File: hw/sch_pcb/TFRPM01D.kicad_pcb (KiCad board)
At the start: 2 copper layers, 37.5 x 19 mm, 23 parts, among them J1 HEADER_1x03, J2 SM04B-GHS-TB, J3 SM04B-GHS-TB, M2 M3, U1 PCF8583, U2 74HC1G14GW, U3 MIC5504-3.3YM5

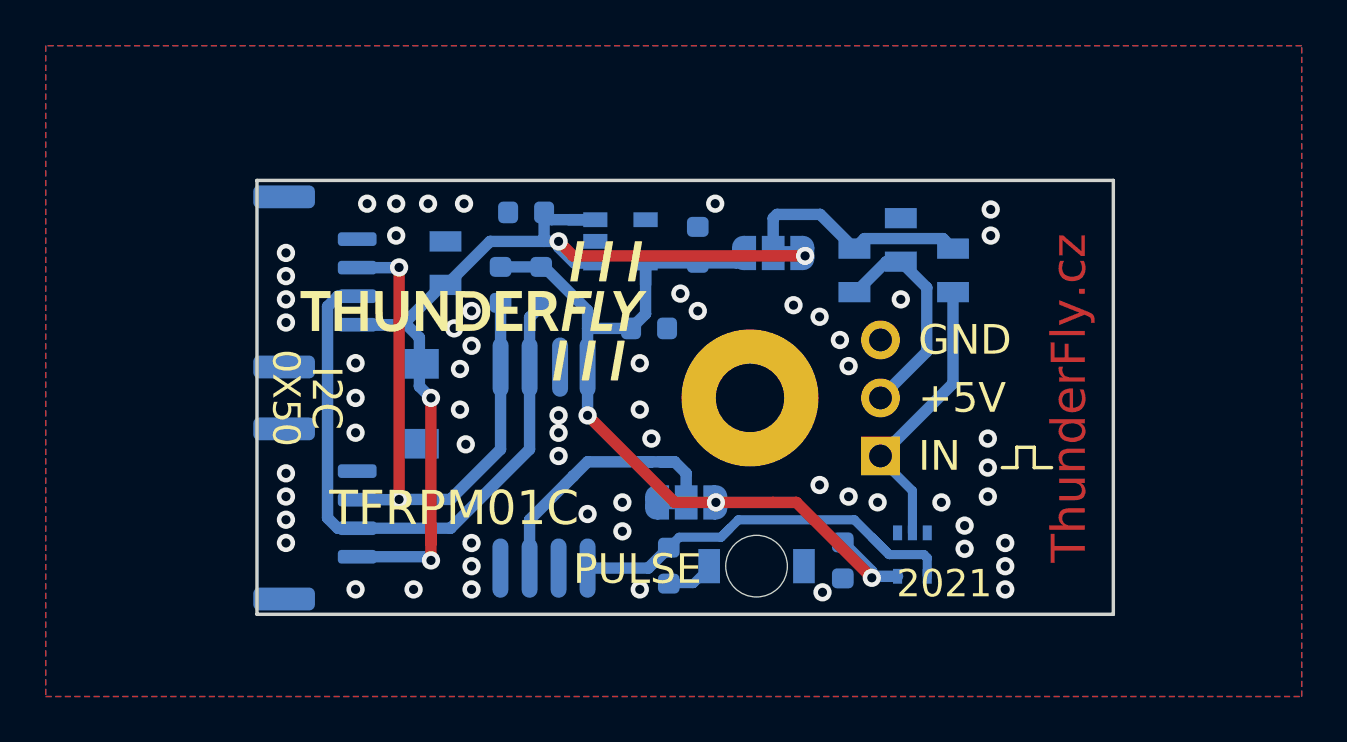
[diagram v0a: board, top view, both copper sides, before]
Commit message: Upraveni PCB, pridani popisku, vyresení #21, #26, urava silkscreenu, vypocet polohy led v openscadu
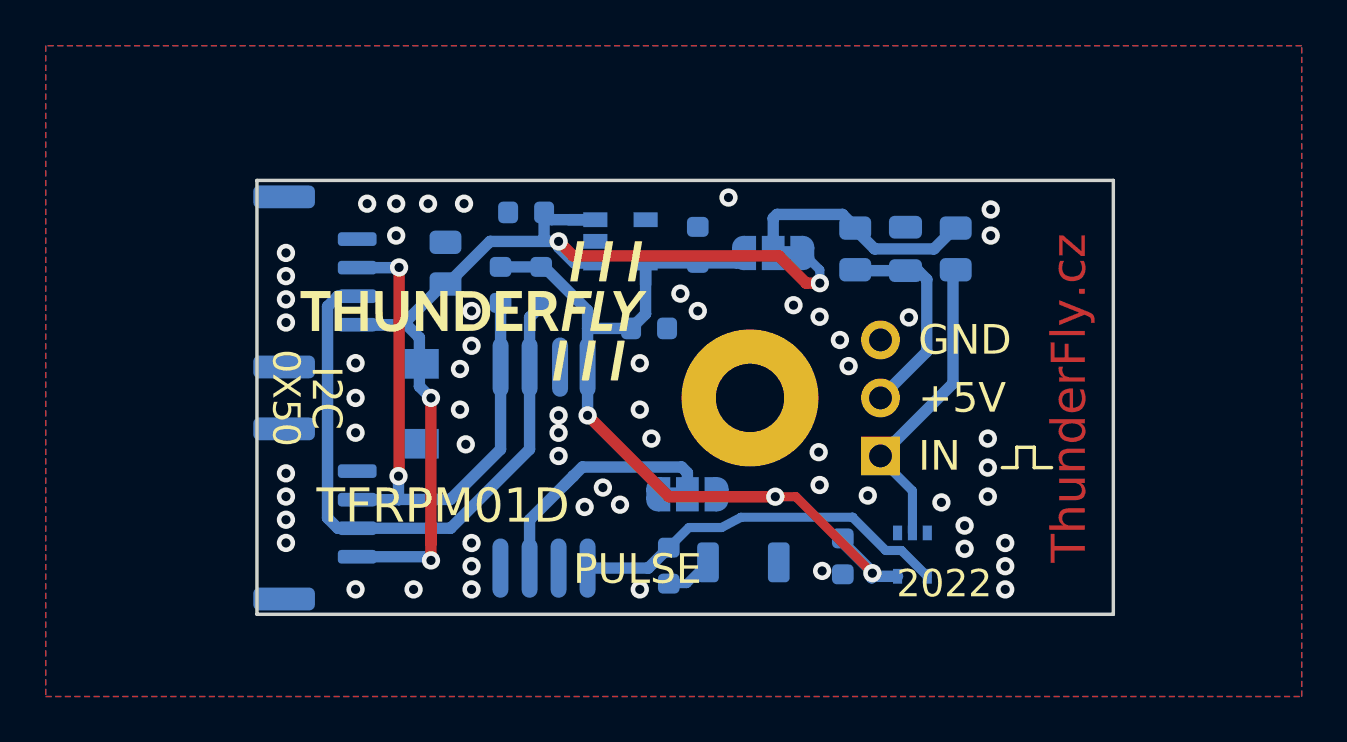
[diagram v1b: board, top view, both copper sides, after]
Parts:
- C2: footprint Mlab_R:SMD-0805 -> Capacitor_SMD:C_0805_2012Metric
- C3, R1, R2: footprint Mlab_R:SMD-0805 -> Resistor_SMD:R_0805_2012Metric
- D1: footprint Mlab_D:Diode-MiniMELF_Standard -> Diode_SMD:D_MiniMELF
- D2: footprint Mlab_D:LED_1206 -> LED_SMD:LED_1206_3216Metric_ReverseMount_Hole1.8x2.4mm
- moved R1 0.95 mm to (141.6, 125.8)
- moved R2 0.94 mm to (137.2, 125.8)
- moved D2 0.60 mm to (132.3, 139.5), turned to 180 degrees
- moved C2 0.44 mm to (139.4, 125.8)
- moved JP1 0.36 mm to (129.8, 136.5)
- moved C6 0.18 mm to (136.7, 139.3)
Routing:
- net +5V: track 45.8 -> 48.6 mm
- net +3V3: track 38.4 -> 40.9 mm
- net Net-(JP1-Pad2): track 13.9 -> 11.7 mm
- net Net-(R4-Pad1): track 18.9 -> 17.1 mm
- net /COUNT: track 12.6 -> 13.6 mm
- net Net-(C2-Pad1): track 9.86 -> 9.32 mm
- net GND: vias 60 -> 59
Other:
- board text added: "2022"
- board text added: "5V"
- board text added: "TFRPM01D"
- board text removed: "2021"
- board text removed: "TFRPM01C"

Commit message: update action, clean repo
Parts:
- removed G***: LOGO, MLAB_LOGA:TF
- added D3: LED GREEN, Diode_SMD:D_1206_3216Metric, B.Cu at (122.3, 139.5)
- added R5: R, Resistor_SMD:R_0603_1608Metric, B.Cu at (127.3, 139.7)
- C1, C4, C5, C6: footprint Mlab_R:SMD-0603 -> Capacitor_SMD:C_0603_1608Metric
- C3: footprint Resistor_SMD:R_0805_2012Metric -> Capacitor_SMD:C_0805_2012Metric
- D1: value ZENER-5.6V -> ZENER-6.2V
- D2: footprint LED_SMD:LED_1206_3216Metric_ReverseMount_Hole1.8x2.4mm -> Diode_SMD:D_1206_3216Metric
- R1: value 470R -> 22k
- R10, R3: footprint Mlab_R:SMD-0603 -> Resistor_SMD:R_0603_1608Metric
- R2: value 100R -> 82R
- R4: value 180R -> 51R; footprint Mlab_R:SMD-0603 -> Resistor_SMD:R_0603_1608Metric
- U2: value 74HC1G14GW -> SN74LVC1G14-Q1
- moved C4 4.29 mm to (118.5, 124.9)
- moved U1 3.04 mm to (123.3, 132.4)
- moved R10 3.00 mm to (125.1, 124.9), turned to 180 degrees
- moved R3 2.48 mm to (121.8, 124.9), turned to 180 degrees
- moved U3 2.14 mm to (129.0, 125.7)
- moved C1 2.00 mm to (132.3, 125.6)
- moved C3 1.99 mm to (118.0, 128.0)
- moved JP2 0.95 mm to (134.5, 125.9), turned to -90 degrees
- moved D1 0.21 mm to (117.9, 132.6)
- turned C5 to -90 degrees
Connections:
- U1 pad 2: (no net) -> unconnected-(U1-Pad2)
- U1 pad 7: (no net) -> unconnected-(U1-Pad7)
- U3 pad 4: (no net) -> unconnected-(U3-Pad4)
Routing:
- net Net-(D3-Pad1): track 0.00 -> 4.00 mm
- net +3V3: track 40.9 -> 44.0 mm
- net +5V: track 48.6 -> 51.5 mm, vias 4 -> 5
- net /SDA: track 25.6 -> 23.2 mm, vias 2 -> 3
- net /SCL: track 27.9 -> 30.3 mm
- net Net-(JP2-Pad2): track 10.7 -> 8.32 mm
- net Net-(JP1-Pad2): track 11.7 -> 10.2 mm
- net Net-(R4-Pad1): track 17.1 -> 17.9 mm
- net GND: vias 59 -> 44

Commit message: procisteni dat
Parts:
- D2, D3: footprint Diode_SMD:D_1206_3216Metric -> LED_SMD:LED_1206_3216Metric_ReverseMount_Hole1.8x2.4mm
- moved J3 0.33 mm to (113.7, 137.1)
- moved J2 0.30 mm to (113.7, 127.5)
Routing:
- net /SCL: track 30.3 -> 29.5 mm
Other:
- board text added: "PWR"

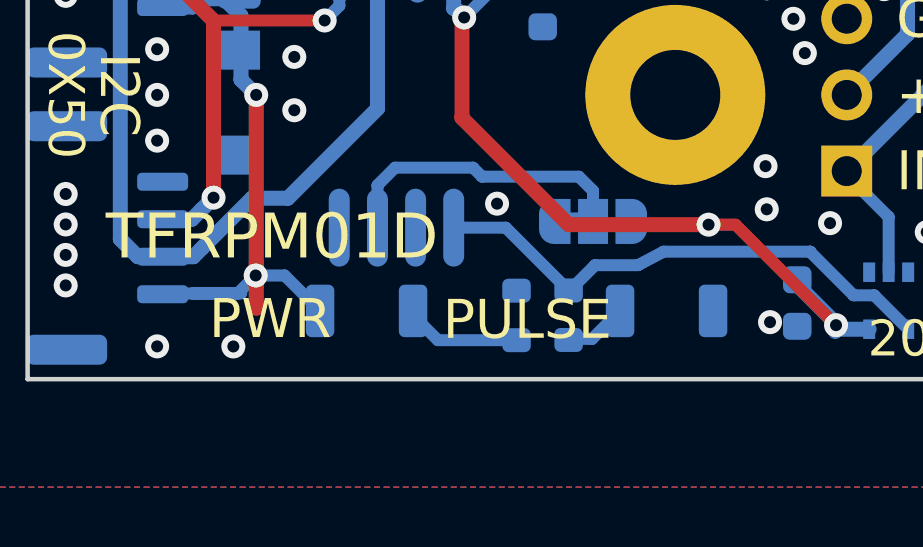
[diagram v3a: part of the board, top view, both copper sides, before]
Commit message: LED case bug fix
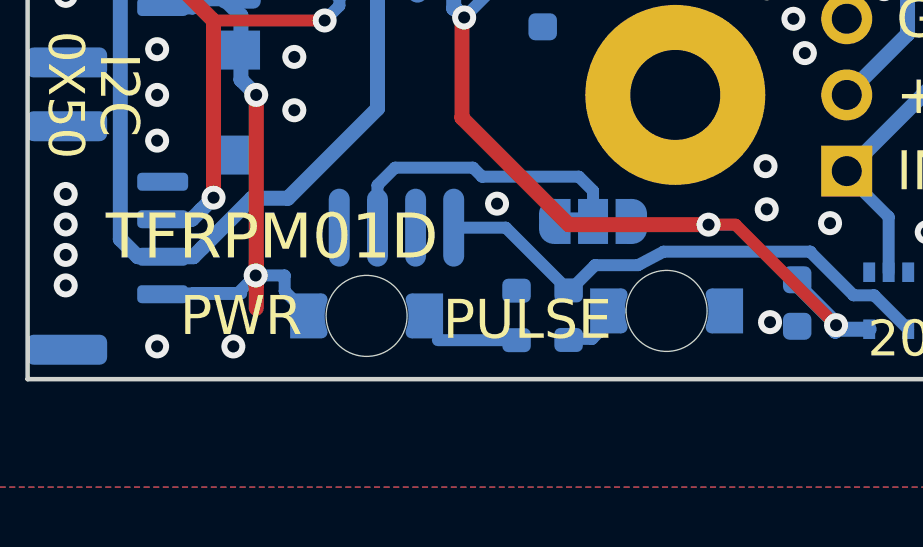
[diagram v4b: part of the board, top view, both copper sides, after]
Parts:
- D2, D3: footprint LED_SMD:LED_1206_3216Metric_ReverseMount_Hole1.8x2.4mm -> Mlab_D:LED_1206
- moved D3 0.17 mm to (122.3, 139.7), turned to 0 degrees
- turned D2 to 0 degrees
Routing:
- net Net-(D3-Pad1): track 4.00 -> 2.62 mm

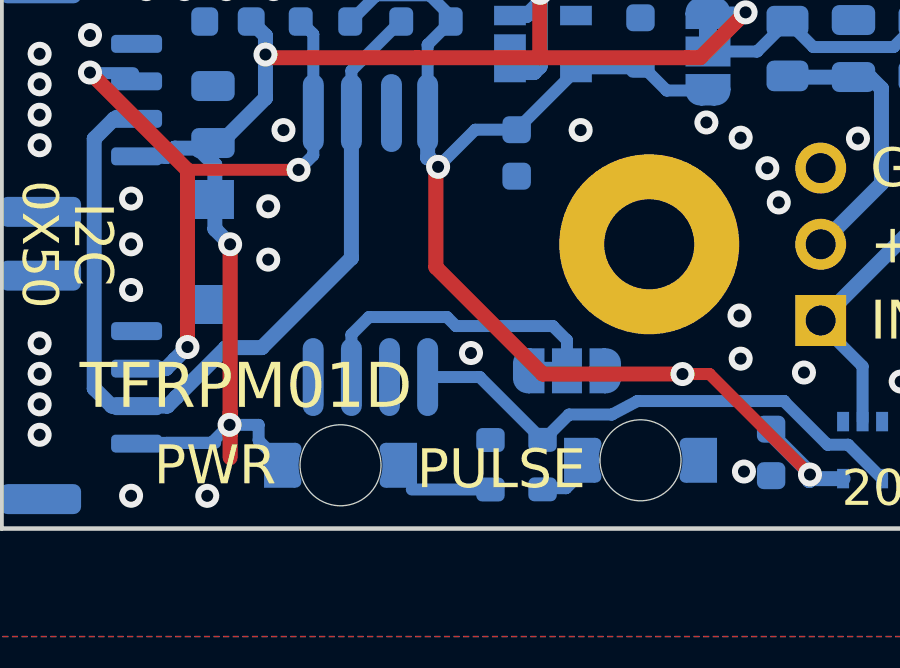
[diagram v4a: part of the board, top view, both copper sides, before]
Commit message: Výměna pouzder LED a D zener
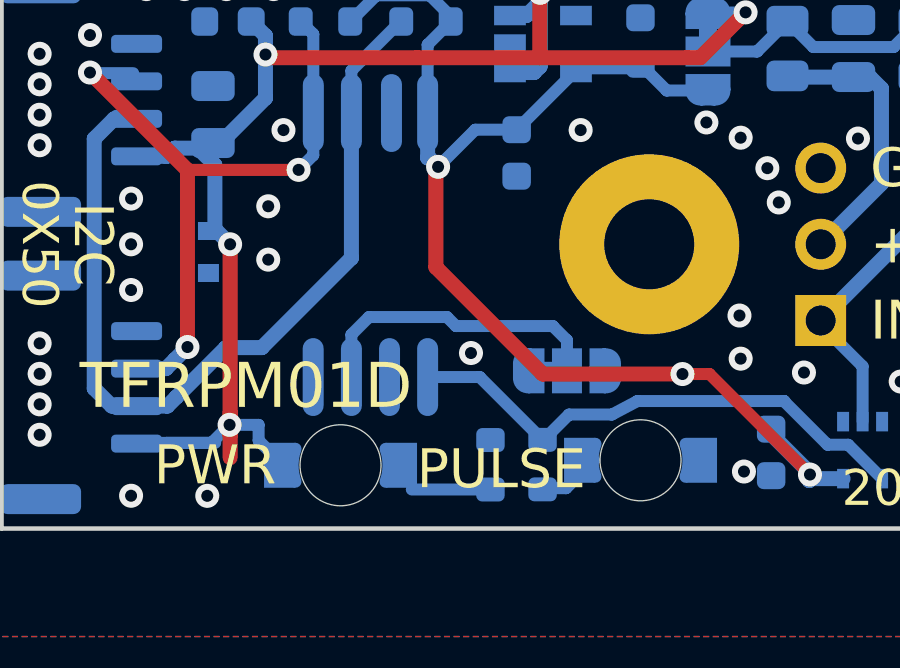
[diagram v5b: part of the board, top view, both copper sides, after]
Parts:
- D1: value ZENER-6.2V -> BZX585-B5V6.115; footprint Diode_SMD:D_MiniMELF -> Diode_SMD:D_SOD-523
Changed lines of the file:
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@@
   (net 14 "unconnected-(U1-Pad7)")
   (net 15 "unconnected-(U3-Pad4)")
-  (footprint "Diode_SMD:D_MiniMELF" (layer "B.Cu")
+  (footprint "Diode_SMD:D_SOD-523" (layer "B.Cu")
     (at 117.896 132.588 -90)
-    (descr "Diode Mini-MELF (SOD-80)")
-    (tags "Diode Mini-MELF (SOD-80)")
-    (property "Sheetfile" "TFRPM01D.kicad_sch")
-    (property "Sheetname" "")
-    (property "UST_ID" "604b0326128750769e5b0f93")
-    (property "UST_id" "")
-    (attr smd)
-    (fp_text reference "D1" (at 3.218 -0.036 180) (layer "B.SilkS")
-      (effects (font (size 0.8 0.8) (thickness 0.1)) (justify mirror))
-    )
-    (fp_text value "ZENER-6.2V" (at 0 -1.75 90) (layer "B.Fab")
-      (effects (font (size 1 1) (thickness 0.15)) (justify mirror))
-    )
-    (fp_text user "${REFERENCE}" (at 0 2 90) (layer "B.Fab")
-      (effects (font (size 1 1) (thickness 0.15)) (justify mirror))
-    )
-    (fp_line (start -2.55 1) (end -2.55 -1) (layer "B.SilkS") (width 0.12))
-    (fp_line (start -2.55 -1) (end 1.75 -1) (layer "B.SilkS") (width 0.12))
-    (fp_line (start 1.75 1) (end -2.55 1) (layer "B.SilkS") (width 0.12))
-    (fp_line (start 2.65 1.1) (end 2.65 -1.1) (layer "B.CrtYd") (width 0.05))
-    (fp_line (start -2.65 1.1) (end 2.65 1.1) (layer "B.CrtYd") (width 0.05))
-    (fp_line (start -2.65 -1.1) (end -2.65 1.1) (layer "B.CrtYd") (width 0.05))
-    (fp_line (start 2.65 -1.1) (end -2.65 -1.1) (layer "B.CrtYd") (width 0.05))
-    (fp_line (start -0.75 0) (end -0.35 0) (layer "B.Fab") (width 0.1))
-    (fp_line (start -0.35 0) (end 0.25 0.4) (layer "B.Fab") (width 0.1))
-    (fp_line (start 0.25 -0.4) (end -0.35 0) (layer "B.Fab") (width 0.1))
-    (fp_line (start -0.35 0) (end -0.35 -0.55) (layer "B.Fab") (width 0.1))
-    (fp_line (start 1.65 0.8) (end 1.65 -0.8) (layer "B.Fab") (width 0.1))
-    (fp_line (start -1.65 -0.8) (end -1.65 0.8) (layer "B.Fab") (width 0.1))
-    (fp_line (start 0.25 0) (end 0.75 0) (layer "B.Fab") (width 0.1))
-    (fp_line (start 1.65 -0.8) (end -1.65 -0.8) (layer "B.Fab") (width 0.1))
-    (fp_line (start -1.65 0.8) (end 1.65 0.8) (layer "B.Fab") (width 0.1))
-    (fp_line (start -0.35 0) (end -0.35 0.55) (layer "B.Fab") (width 0.1))
-    (fp_line (start 0.25 0.4) (end 0.25 -0.4) (layer "B.Fab") (width 0.1))
-    (pad "1" smd rect (at -1.75 0 270) (size 1.3 1.7) (layers "B.Cu" "B.Paste" "B.Mask")
+    (descr "http://www.diodes.com/datasheets/ap02001.pdf p.144")
+    (tags "Diode SOD523")
+    (property "Sheetfile" "TFRPM01D.kicad_sch")
+    (property "Sheetname" "")
+    (property "UST_ID" "60879d38128750769ee58e48")
+    (property "UST_id" "")
+    (attr smd)
+    (fp_text reference "D1" (at 0 1.3 90) (layer "B.SilkS")
+      (effects (font (size 1 1) (thickness 0.15)) (justify mirror))
+    )
+    (fp_text value "BZX585-B5V6.115" (at 0 -1.4 90) (layer "B.Fab")
+      (effects (font (size 1 1) (thickness 0.15)) (justify mirror))
+    )
+    (fp_text user "${REFERENCE}" (at 0 1.3 90) (layer "B.Fab")
+      (effects (font (size 1 1) (thickness 0.15)) (justify mirror))
+    )
+    (fp_line (start 0.7 -0.6) (end -1.15 -0.6) (layer "B.SilkS") (width 0.12))
+    (fp_line (start 0.7 0.6) (end -1.15 0.6) (layer "B.SilkS") (width 0.12))
+    (fp_line (start -1.15 0.6) (end -1.15 -0.6) (layer "B.SilkS") (width 0.12))
+    (fp_line (start 1.25 0.7) (end 1.25 -0.7) (layer "B.CrtYd") (width 0.05))
+    (fp_line (start -1.25 0.7) (end 1.25 0.7) (layer "B.CrtYd") (width 0.05))
+    (fp_line (start -1.25 -0.7) (end -1.25 0.7) (layer "B.CrtYd") (width 0.05))
+    (fp_line (start 1.25 -0.7) (end -1.25 -0.7) (layer "B.CrtYd") (width 0.05))
+    (fp_line (start 0.1 -0.2) (end 0.1 0.2) (layer "B.Fab") (width 0.1))
+    (fp_line (start 0.1 0.2) (end -0.2 0) (layer "B.Fab") (width 0.1))
+    (fp_line (start 0.1 0) (end 0.25 0) (layer "B.Fab") (width 0.1))
+    (fp_line (start -0.2 -0.2) (end -0.2 0.2) (layer "B.Fab") (width 0.1))
+    (fp_line (start -0.2 0) (end 0.1 -0.2) (layer "B.Fab") (width 0.1))
+    (fp_line (start -0.65 0.45) (end 0.65 0.45) (layer "B.Fab") (width 0.1))
+    (fp_line (start -0.65 -0.45) (end -0.65 0.45) (layer "B.Fab") (width 0.1))
+    (fp_line (start -0.2 0) (end -0.35 0) (layer "B.Fab") (width 0.1))
+    (fp_line (start 0.65 -0.45) (end -0.65 -0.45) (layer "B.Fab") (width 0.1))
+    (fp_line (start 0.65 0.45) (end 0.65 -0.45) (layer "B.Fab") (width 0.1))
+    (pad "1" smd rect (at -0.7 0 90) (size 0.6 0.7) (layers "B.Cu" "B.Paste" "B.Mask")
       (net 5 "+5V") (pinfunction "K") (pintype "passive"))
-    (pad "2" smd rect (at 1.75 0 270) (size 1.3 1.7) (layers "B.Cu" "B.Paste" "B.Mask")
+    (pad "2" smd rect (at 0.7 0 90) (size 0.6 0.7) (layers "B.Cu" "B.Paste" "B.Mask")
       (net 1 "GND") (pinfunction "A") (pintype "passive"))
-    (model "${KICAD6_3DMODEL_DIR}/Diode_SMD.3dshapes/D_MiniMELF.wrl"
+    (model "${KICAD6_3DMODEL_DIR}/Diode_SMD.3dshapes/D_SOD-523.wrl"
       (offset (xyz 0 0 0))
       (scale (xyz 1 1 1))
@@
       (options (clearance outline) (anchor rect))
       (primitives
-    (gr_arc (start 0.404306 0.548105) (mid 0.307346 -0.001009) (end 0.405 -0.55) (width 0.4))
+    (gr_arc (start 0.404306 0.548105) (mid 0.307346 -0.001009) (end 0.405 -0.549999) (width 0.4))
         (gr_poly (pts
+            (xy 0.405 0.75)
+            (xy -0.645 0.75)
+            (xy -0.645 -0.75)
             (xy 0.405 -0.75)
-            (xy -0.645 -0.75)
-            (xy -0.645 0.75)
-            (xy 0.405 0.75)
           ) (width 0) (fill yes))
       ))
@@
       (options (clearance outline) (anchor rect))
       (primitives
-    (gr_arc (start 0.404306 0.548105) (mid 0.307346 -0.001009) (end 0.405 -0.55) (width 0.4))
+    (gr_arc (start 0.404306 0.548105) (mid 0.307346 -0.001009) (end 0.405 -0.549999) (width 0.4))
         (gr_poly (pts
+            (xy 0.405 0.75)
+            (xy -0.645 0.75)
+            (xy -0.645 -0.75)
             (xy 0.405 -0.75)
-            (xy -0.645 -0.75)
-            (xy -0.645 0.75)
-            (xy 0.405 0.75)
           ) (width 0) (fill yes))
       ))
@@
       (options (clearance outline) (anchor rect))
       (primitives
-    (gr_arc (start 0.404306 0.548105) (mid 0.307346 -0.001009) (end 0.405 -0.55) (width 0.4))
+    (gr_arc (start 0.404306 0.548105) (mid 0.307346 -0.001009) (end 0.405 -0.549999) (width 0.4))
         (gr_poly (pts
+            (xy 0.405 0.75)
+            (xy -0.645 0.75)
+            (xy -0.645 -0.75)
             (xy 0.405 -0.75)
-            (xy -0.645 -0.75)
-            (xy -0.645 0.75)
-            (xy 0.405 0.75)
           ) (width 0) (fill yes))
       ))
@@
       (options (clearance outline) (anchor rect))
       (primitives
-    (gr_arc (start 0.404306 0.548105) (mid 0.307346 -0.001009) (end 0.405 -0.55) (width 0.4))
+    (gr_arc (start 0.404306 0.548105) (mid 0.307346 -0.001009) (end 0.405 -0.549999) (width 0.4))
         (gr_poly (pts
+            (xy 0.405 0.75)
+            (xy -0.645 0.75)
+            (xy -0.645 -0.75)
             (xy 0.405 -0.75)
-            (xy -0.645 -0.75)
-            (xy -0.645 0.75)
-            (xy 0.405 0.75)
           ) (width 0) (fill yes))
       ))
